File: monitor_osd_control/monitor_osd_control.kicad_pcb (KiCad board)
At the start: 2 copper layers, 50 x 58 mm, 21 parts, among them J1 Conn_01x09, J2 Conn_01x09, J3 Conn_01x05, J4 Conn_01x05, SW1 SW_Push, SW2 SW_Push, SW3 SW_Push, SW4 SW_Push, SW5 SW_Push, SW6 SW_Push, U1 TSSP58038

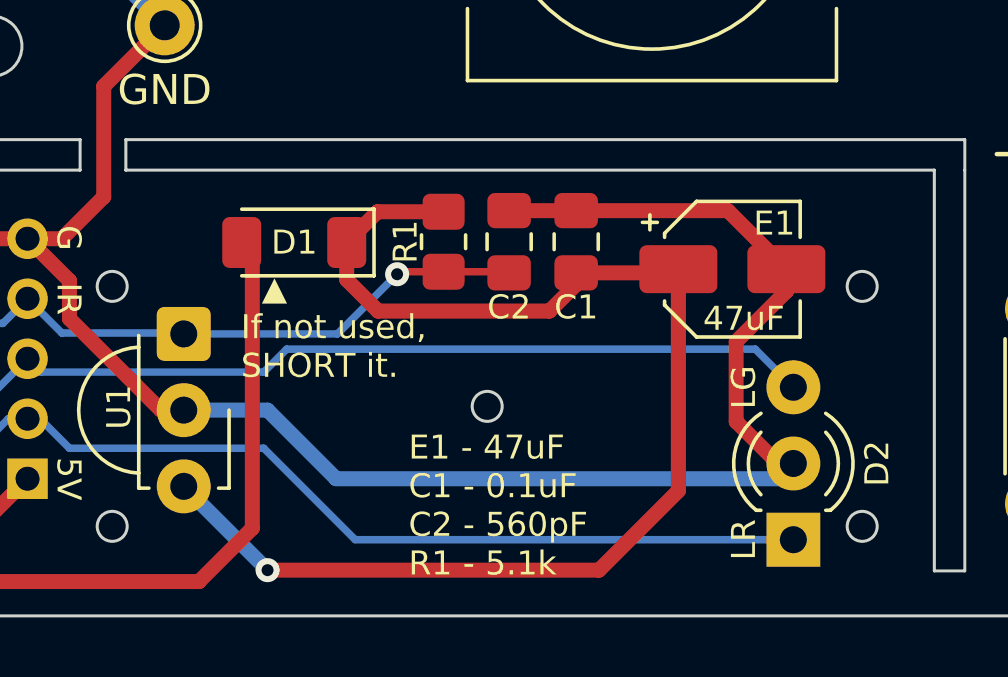
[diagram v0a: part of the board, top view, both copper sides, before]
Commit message: 캐패시터 크기 변경
Signed-off-by: Ju, Gyeong-min <jcmh74@gmail.com>
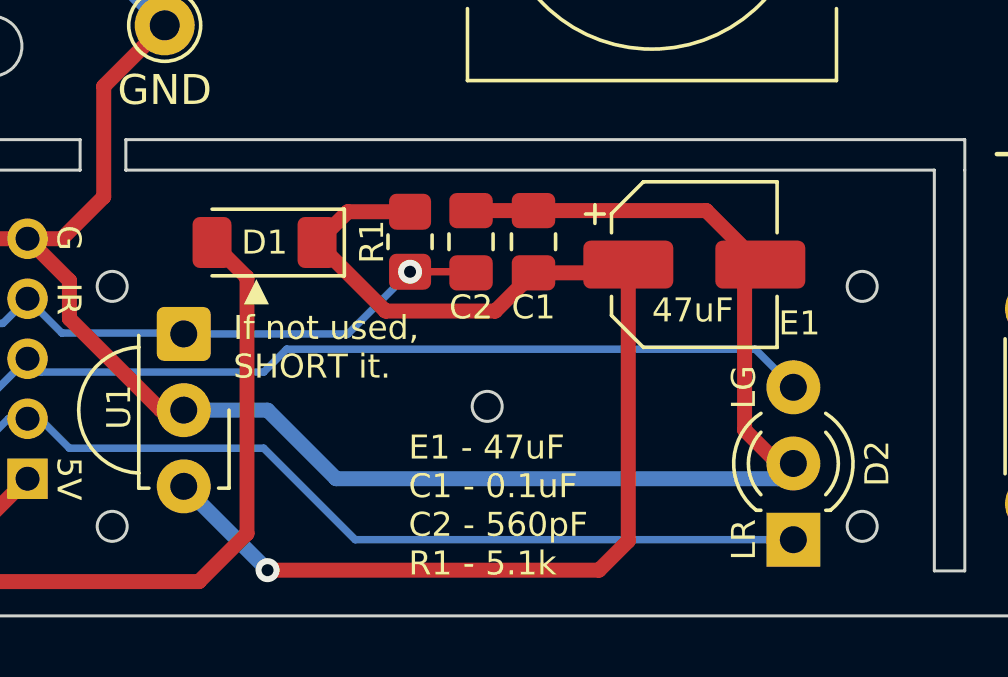
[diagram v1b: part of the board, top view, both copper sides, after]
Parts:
- E1: footprint Capacitor_SMD:CP_Elec_4x5.4 -> Capacitor_SMD:CP_Elec_5x5.4
- moved C1 1.42 mm to (149.7, 107.3)
- moved E1 1.28 mm to (155.1, 108.1)
- moved C2 1.27 mm to (147.6, 107.3)
- moved R1 1.12 mm to (145.6, 107.3)
- moved D1 0.99 mm to (140.7, 107.3)
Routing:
- net Net-(D1-K): track 43.3 -> 41.1 mm
- net /IRIN: track 20.3 -> 19.0 mm

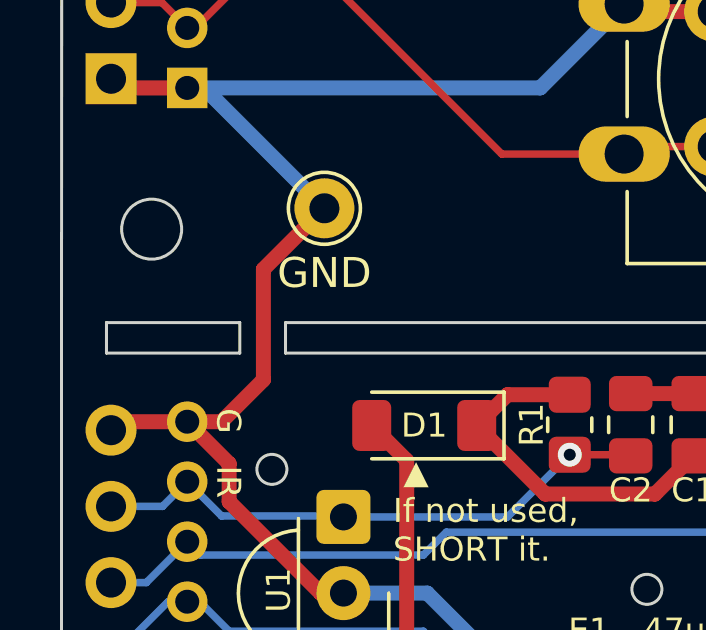
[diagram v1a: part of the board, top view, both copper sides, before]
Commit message: GND 면적 증가
Signed-off-by: Ju, Gyeong-min <jcmh74@gmail.com>
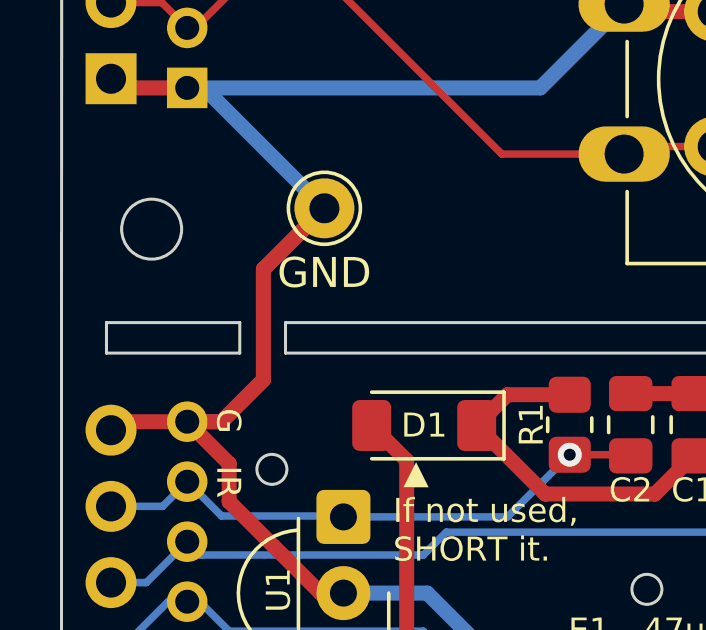
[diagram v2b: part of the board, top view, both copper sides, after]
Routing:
- net GND: track 226.9 -> 236.6 mm
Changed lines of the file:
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@@
   (segment (start 156.7434 108.5752) (end 156.7434 113.5634) (width 0.5) (layer "F.Cu") (net 7))
   (segment (start 164.4076 88.7264) (end 164.156 88.978) (width 0.5) (layer "F.Cu") (net 7))
+  (segment (start 135.382 105.791) (end 135.382 102.108) (width 0.5) (layer "B.Cu") (net 7))
   (segment (start 159.906 93.268) (end 164.156 89.018) (width 0.5) (layer "B.Cu") (net 7))
+  (segment (start 133.984 107.189) (end 135.382 105.791) (width 0.5) (layer "B.Cu") (net 7))
+  (segment (start 135.382 102.108) (end 137.414 100.076) (width 0.5) (layer "B.Cu") (net 7))
   (segment (start 157.861 115.189) (end 158.369 114.681) (width 0.5) (layer "B.Cu") (net 7))
   (segment (start 137.16 70.866) (end 137.16 71.2978) (width 0.5) (layer "B.Cu") (net 7))
@@
   (segment (start 138.049 112.903) (end 140.843 112.903) (width 0.5) (layer "B.Cu") (net 7))
   (segment (start 142.3502 76.488) (end 143.176 76.488) (width 0.5) (layer "B.Cu") (net 7))
+  (segment (start 132.842 107.189) (end 133.984 107.189) (width 0.5) (layer "B.Cu") (net 7))
   (segment (start 164.156 88.978) (end 160.436 85.258) (width 0.5) (layer "B.Cu") (net 7))
   (segment (start 133.4008 96.0628) (end 132.842 96.0628) (width 0.5) (layer "B.Cu") (net 7))
